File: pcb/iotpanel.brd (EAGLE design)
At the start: 48.2 x 49.2 mm, 33 parts, among them IC1 IC_CPLD_XC2C32A, IC4 REG1117, IC5 REG1117

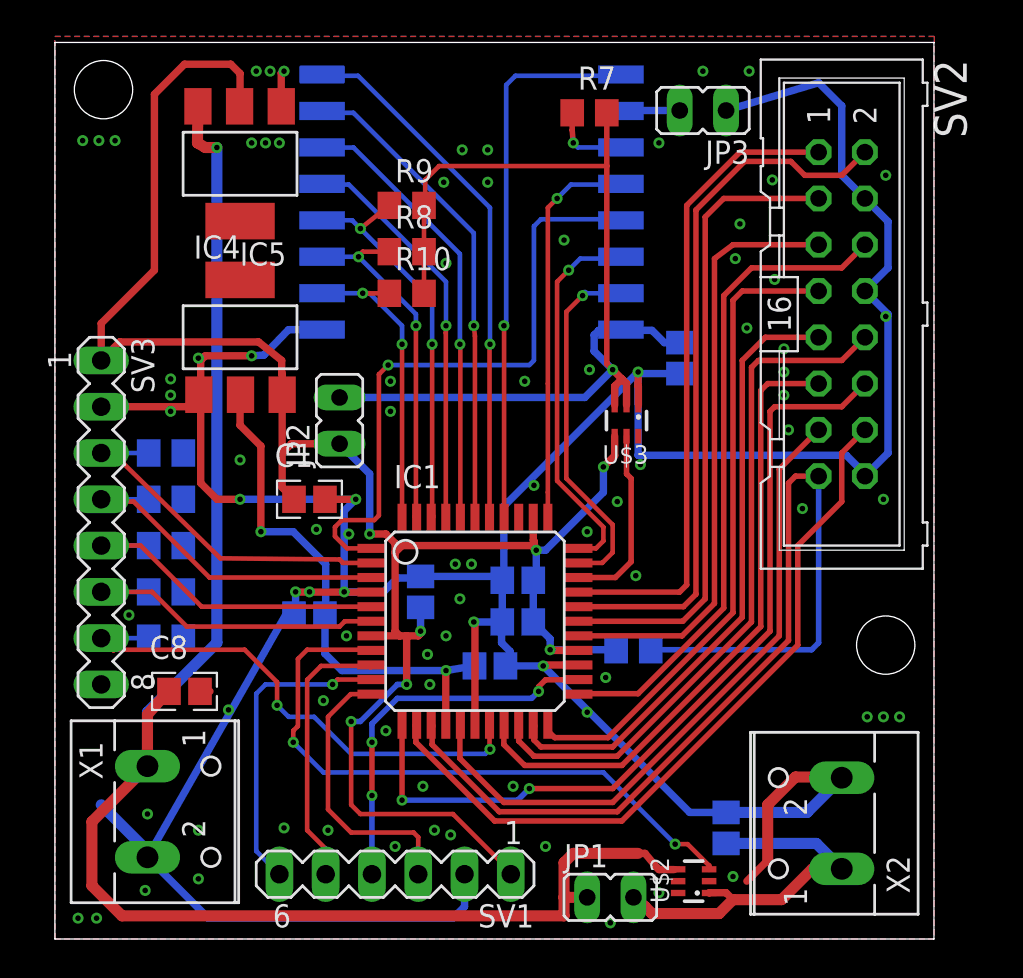
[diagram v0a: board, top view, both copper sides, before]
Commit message: Add v1.1 board
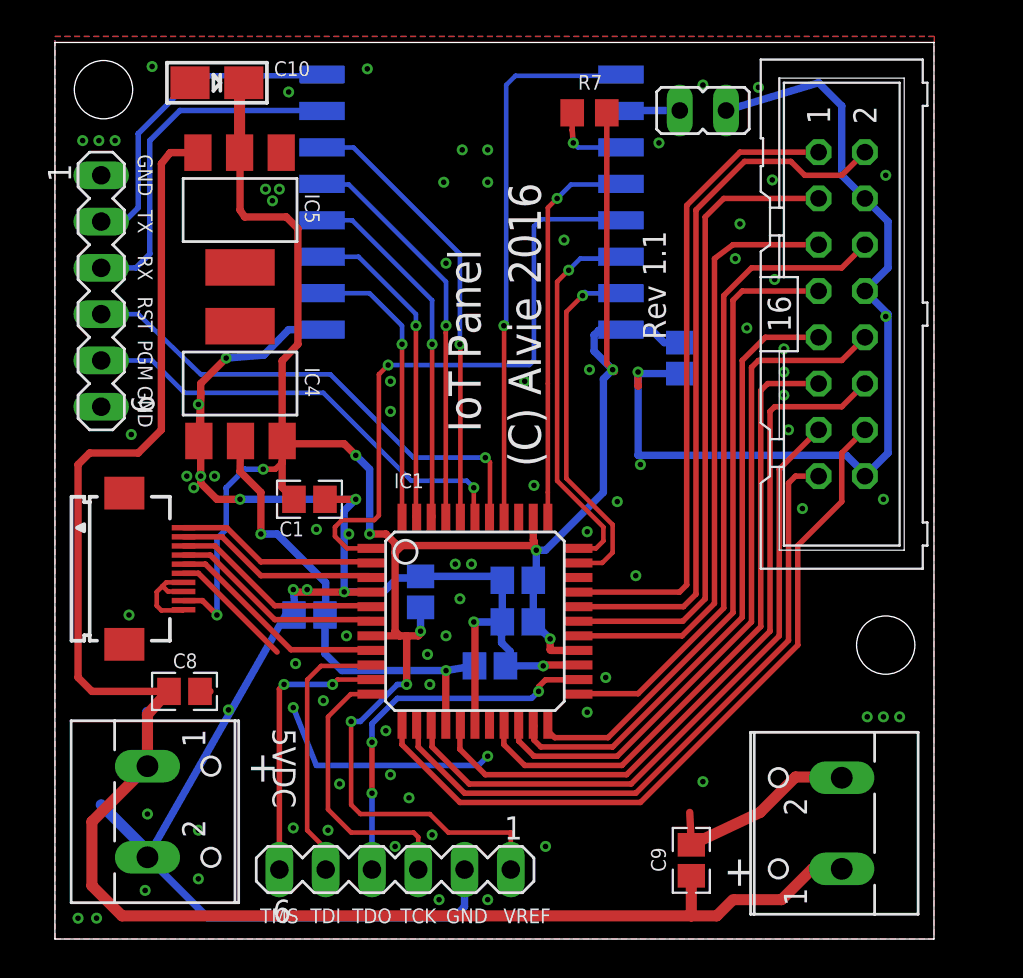
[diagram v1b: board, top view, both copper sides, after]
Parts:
- removed JP1, JP2: (no value), jumper:JP1
- removed R1, R2, R3, R4, R5, R6: 10k, rcl:R0805
- removed R10, R8, R9: DNP, rcl:R0805
- removed SV3: (no value), con-lstb:MA08-1
- removed U$2: MIC9406XBC6, alvie:SC70-6L
- removed U$3: SI1867DL, alvie:SC70-6L
- added C10: (no value), microbuilder:EIA3216-18/A-W
- added SV4: (no value), con-lstb:MA06-1
- added X3: FH12-10S-0.5SH, con-hirose:FH12-10S-0.5SH
- moved C9 2.61 mm to (34.9, 4.32), flipped to the top
- moved IC4 2.54 mm to (10.2, 30.5)
- moved IC5 2.54 mm to (10.2, 40.0)
- moved SV1 0.25 mm to (18.7, 3.81)
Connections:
- removed net ESPEN: IC1.31, U$3.5
- removed net ESPVCC: C3.1, JP2.2, R10.2, R7.2, R8.2, R9.2, U$1.VCC, U$3.2, U$3.3
- removed net PANELVCC: C9.1, JP1.2, U$2.1, X2.1
- removed net PANEL_EN: IC1.8, U$2.3
- new net NPGM: IC1.39, SV4.5
- new net NRST: IC1.38, SV4.4
- net +3V3: now also C10.+, C3.1, R7.2, U$1.VCC, X3.9; no longer JP2.1, R6.1, SV3.1, U$3.4
- net +5V: now also C9.1, X2.1; no longer JP1.1, U$2.4
- net CLK: now also IC1.14; no longer IC1.16
- net D: now also IC1.16; no longer IC1.12
- net ESP_GPIO0: no longer R9.1
- net ESP_GPIO15: no longer R10.1
- net ESP_GPIO2: no longer R8.1
- net ESP_RX: now also SV4.3; no longer IC1.39
- net ESP_TX: now also SV4.2; no longer IC1.38
- net GND: now also C10.-, SV4.1, SV4.6, X3.10, X3.6, X3.7, X3.8; no longer R1.1, R2.1, R3.1, R4.1, R5.1, SV3.2, SV3.8, U$2.2, U$2.5, U$3.1
- net OE: now also IC1.13; no longer IC1.14, R6.2
- net STB: now also IC1.12; no longer IC1.13
- net USR2: now also IC1.8, X3.5; no longer IC1.18, R5.2, SV3.7
- net USR3: now also X3.4; no longer R4.2, SV3.6
- net USR4: now also X3.3; no longer R3.2, SV3.5
- net USR5: now also X3.2; no longer R2.2, SV3.4
- net USR6: now also X3.1; no longer R1.2, SV3.3
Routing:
- net ESPVCC: track 58.1 -> 0.00 mm, vias 1 -> 0
- net PANEL_EN: track 34.7 -> 0.00 mm, vias 2 -> 0
- net NRST: track 0.00 -> 27.7 mm, vias 0 -> 1
- net NPGM: track 0.00 -> 25.0 mm, vias 0 -> 1
- net +3V3: track 112.6 -> 134.2 mm, vias 7 -> 10
- net PANELVCC: track 21.2 -> 0.00 mm
- net OE: track 55.0 -> 36.5 mm
- net USR2: track 28.8 -> 12.3 mm, vias 2 -> 0
- net GND: track 205.8 -> 191.7 mm, vias 89 -> 93
- net ESP_TX: track 29.2 -> 17.8 mm, vias 1 -> 0
- net +5V: track 88.7 -> 99.7 mm, vias 1 -> 0
- net ESPEN: track 10.2 -> 0.00 mm
- net USR6: track 19.9 -> 11.1 mm
- net USR5: track 19.2 -> 11.2 mm
- net ESP_RX: track 26.7 -> 19.4 mm, vias 1 -> 0
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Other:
- board text added: "(C) Alvie 2016"
- board text added: "5VDC"
- board text added: "PGM"
- board text added: "RST"
- board text added: "RX"
- board text added: "Rev 1.1"
- board text added: "TX"
- board text removed: "(C) Alvie 2015"
- board text removed: "+3v3"
